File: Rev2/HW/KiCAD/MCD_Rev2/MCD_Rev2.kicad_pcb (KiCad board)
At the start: 2 copper layers, 196.3 x 114.9 mm, 76 parts, among them J1 DBUS_LOW, J2 DBUS_HIGH, J3 ABUS, J4 POWER, J5 JTAG, J6 Conn_01x02_Male, J7 DUART A, J8 DUART B, SW1 SW_Push, U1 XC9572XL-PC44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

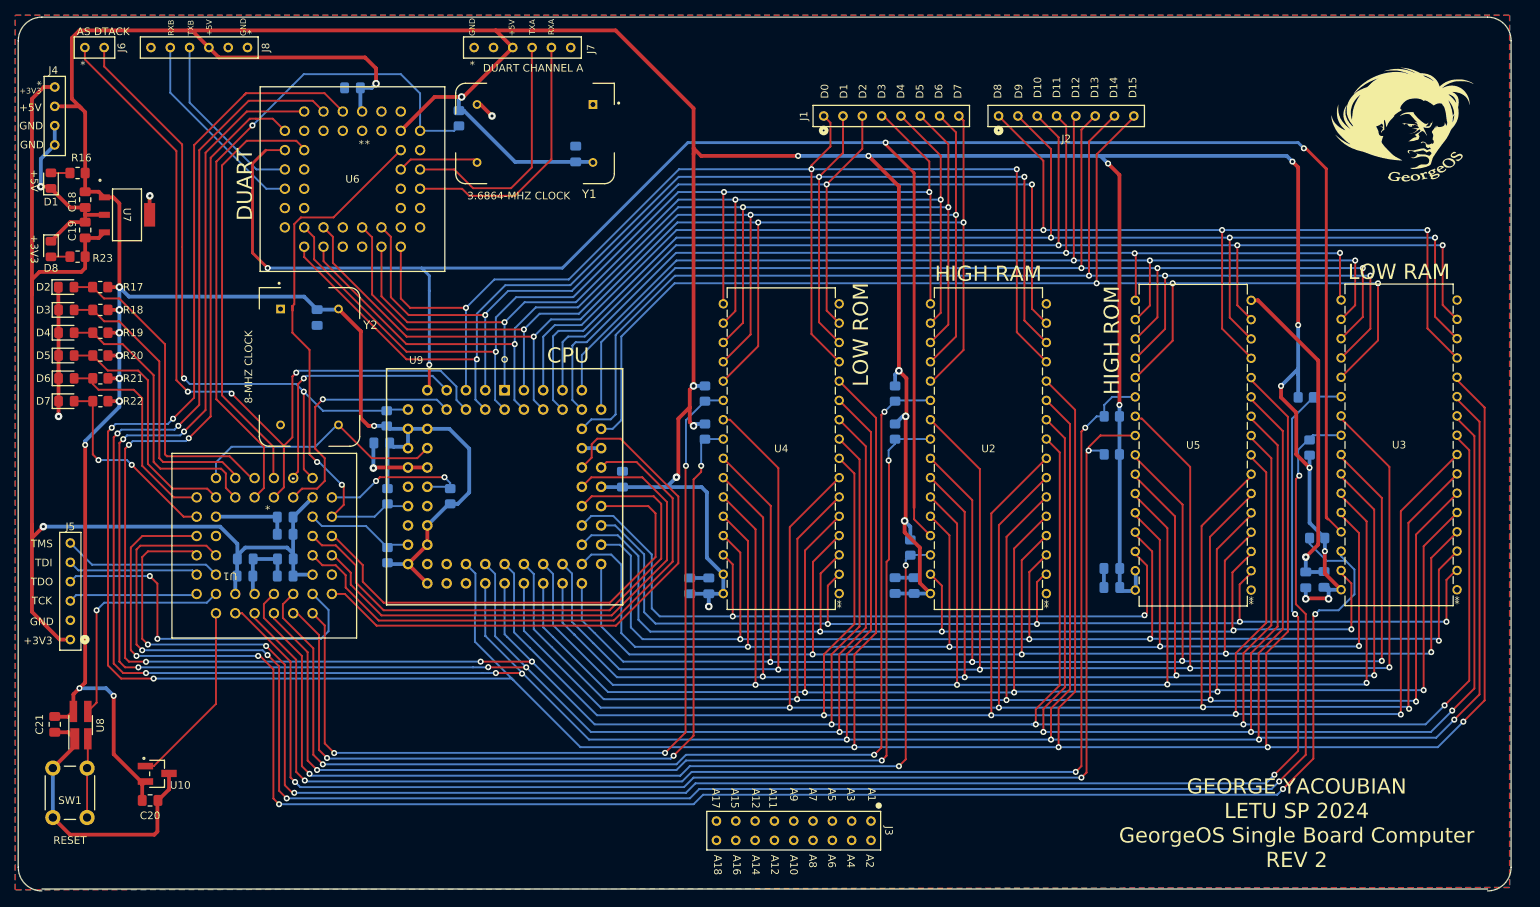
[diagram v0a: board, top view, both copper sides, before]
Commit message: started via stitching
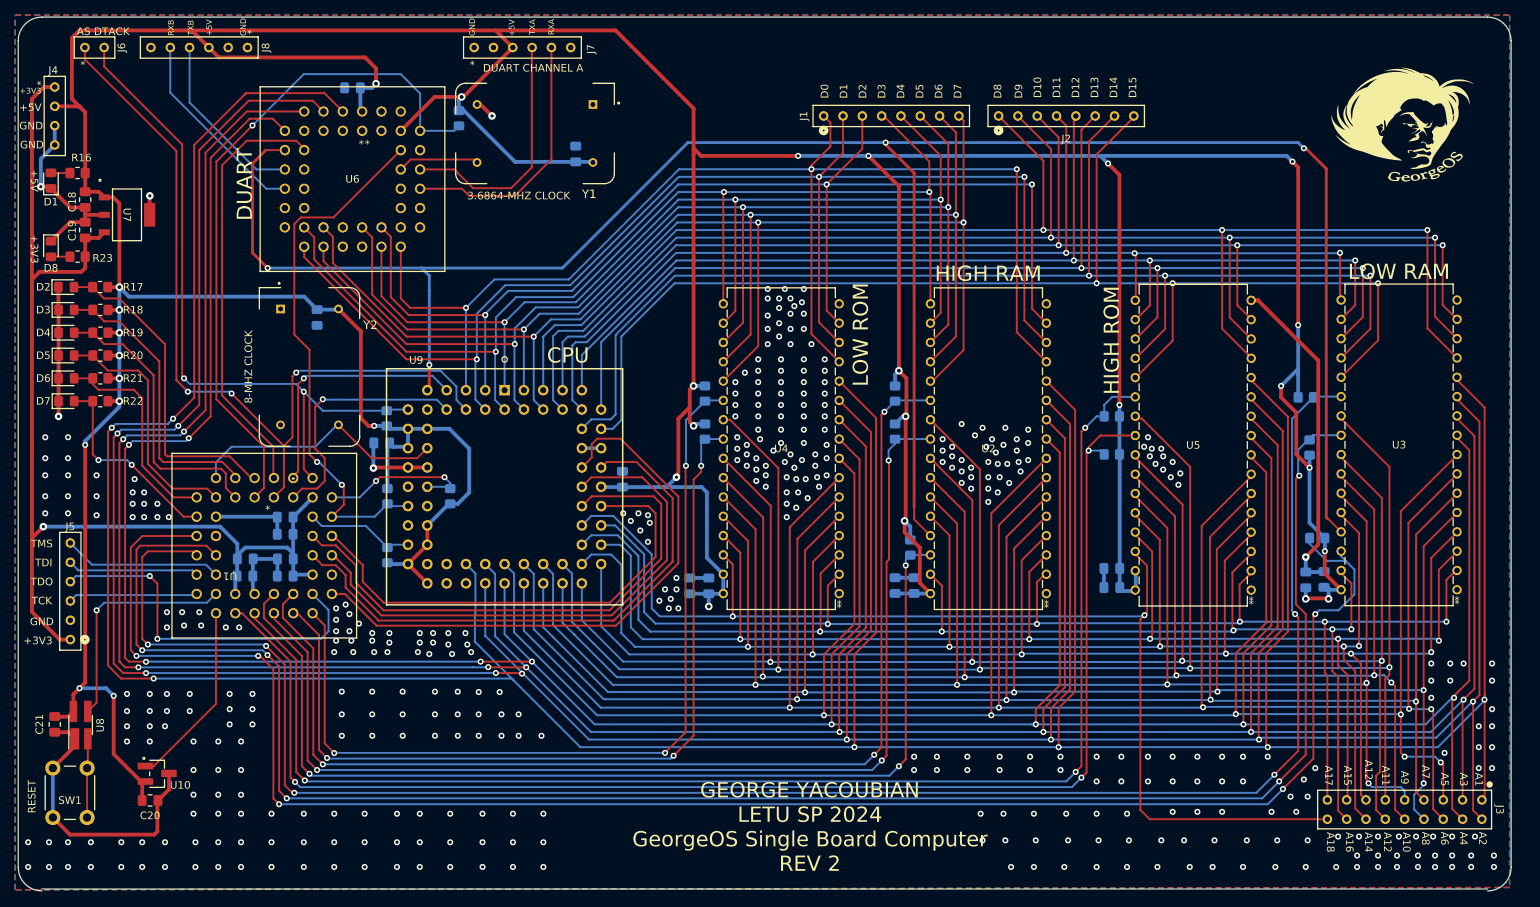
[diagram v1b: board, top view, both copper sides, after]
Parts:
- moved J3 80.4 mm to (283.0, 175.7)
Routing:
- net A18: track 101.7 -> 152.6 mm
- net A16: track 150.6 -> 176.3 mm, vias 4 -> 5
- net A14: track 186.8 -> 210.7 mm, vias 4 -> 5
- net A17: track 149.6 -> 173.2 mm, vias 4 -> 5
- net A15: track 174.8 -> 196.5 mm, vias 4 -> 5
- net A12: track 229.5 -> 251.1 mm
- net A10: track 228.1 -> 249.5 mm, vias 4 -> 5
- net A13: track 187.1 -> 207.2 mm, vias 4 -> 5
- net A9: track 224.2 -> 243.9 mm, vias 4 -> 5
- net A6: track 259.2 -> 277.2 mm, vias 4 -> 5
- net A8: track 225.2 -> 243.2 mm, vias 4 -> 5
- net A11: track 262.2 -> 279.9 mm
- net A4: track 434.9 -> 451.7 mm
- net A2: track 478.5 -> 494.5 mm
- net A5: track 277.0 -> 292.9 mm, vias 4 -> 6
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
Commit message: finished signals and power, need to via stitch
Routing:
- net GND: track 170.4 -> 108.9 mm, vias 428 -> 8
- net RAMHCE: track 242.1 -> 294.6 mm, vias 5 -> 3
- net RAMHCE2: track 237.3 -> 227.3 mm
- net RAMHOE: track 245.1 -> 235.5 mm
- net ROMLCE: track 113.9 -> 104.8 mm, vias 3 -> 1
- net ROMHOE: track 183.1 -> 174.2 mm, vias 3 -> 1
- net ROMLOE: track 112.7 -> 103.8 mm, vias 3 -> 1
- net ROMHCE: track 181.6 -> 173.0 mm, vias 3 -> 1
- net RAMLCE2: track 135.8 -> 127.3 mm, vias 3 -> 1
- net RAMLOE: track 145.4 -> 137.0 mm, vias 3 -> 1
- net RAMLCE: track 150.8 -> 142.6 mm, vias 3 -> 1
- net +5V: track 776.9 -> 771.7 mm, vias 30 -> 27
- net LED4: track 28.8 -> 28.2 mm
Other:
- board size 196.3 x 114.9 mm -> 196.3 x 114.7 mm
- board text added: "GEORGE YACOUBIAN LETU SU 2024 GeorgeOS Single Board Computer REV 3"
- board text removed: "GEORGE YACOUBIAN LETU SP 2024 GeorgeOS Single Board Computer REV 2"

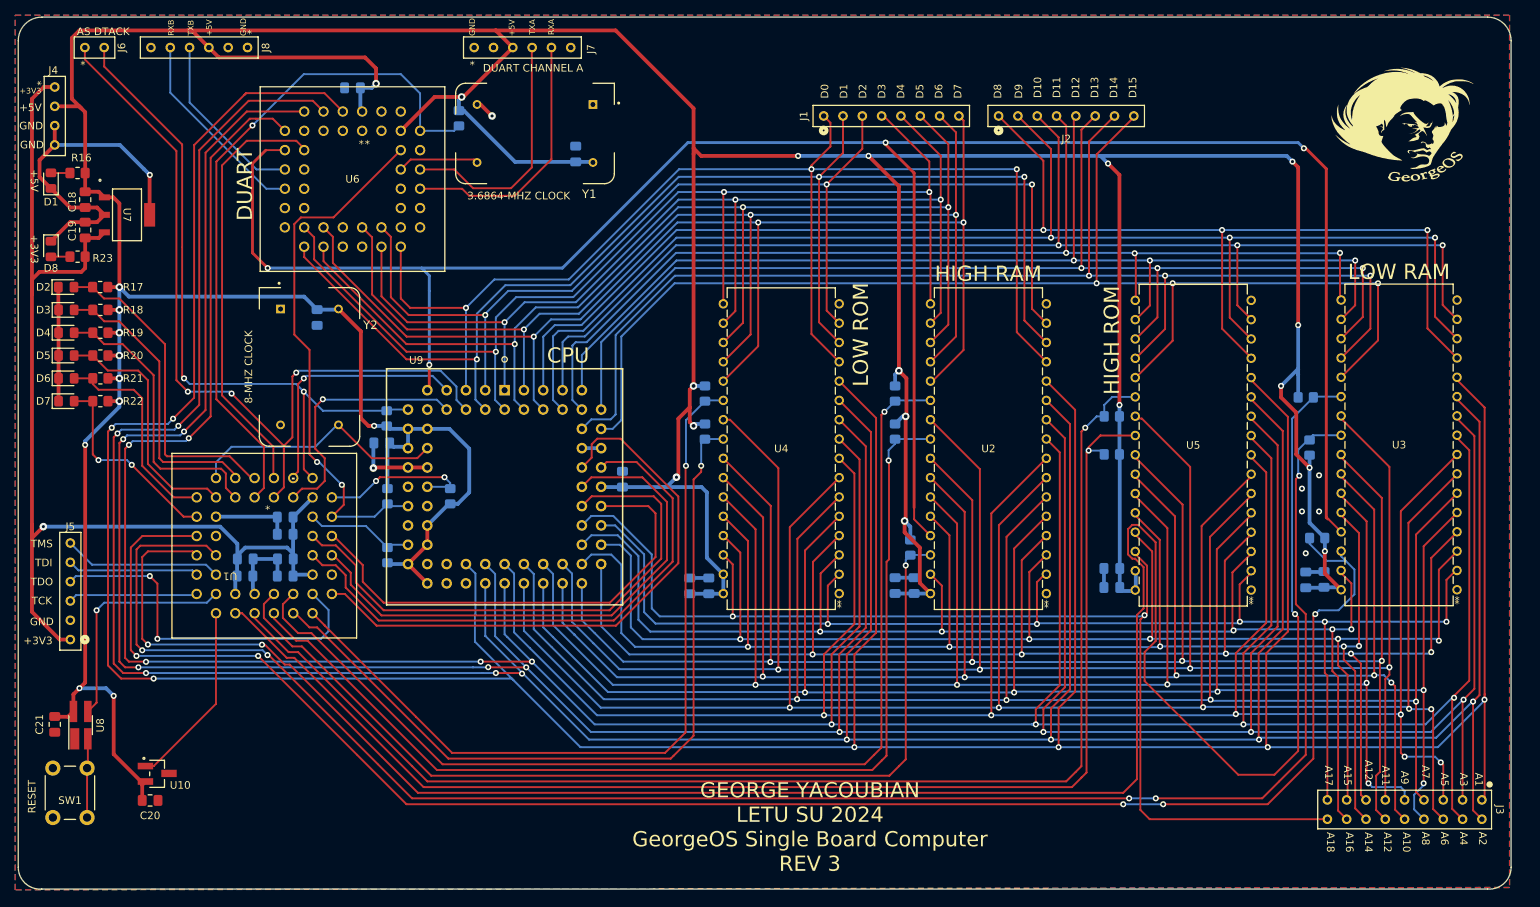
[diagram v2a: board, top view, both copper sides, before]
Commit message: spaced out traces
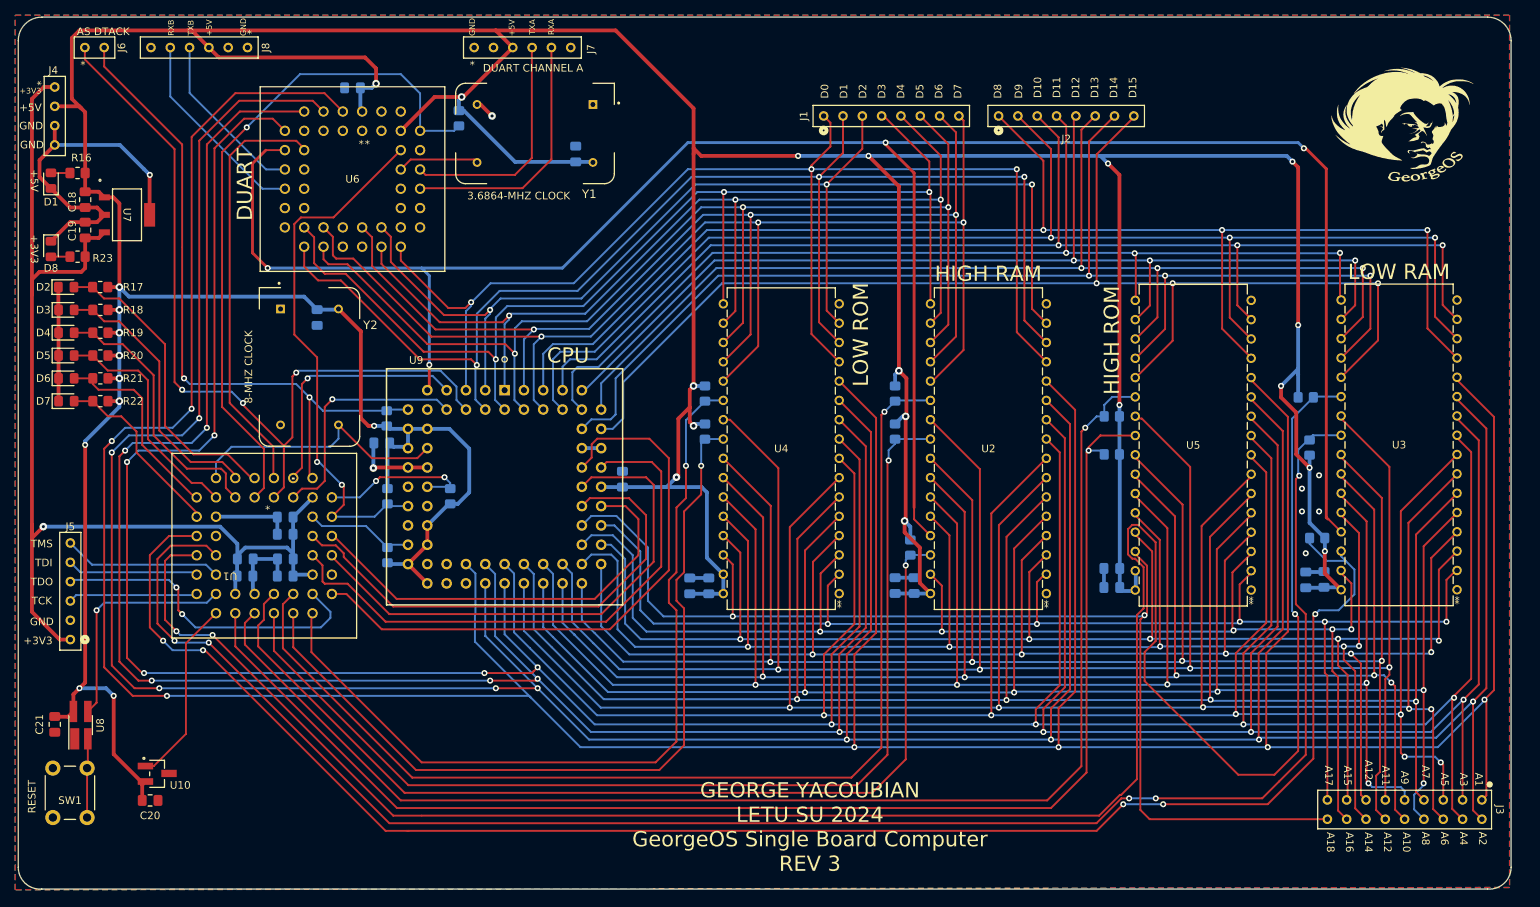
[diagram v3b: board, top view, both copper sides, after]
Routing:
- net A19: track 63.3 -> 56.5 mm
- net A20: track 72.6 -> 66.1 mm
- net ROMHCE: track 173.0 -> 178.9 mm
- net RAMHCE: track 294.6 -> 288.9 mm
- net A1: track 518.1 -> 523.3 mm
- net RAMHOE: track 235.5 -> 230.4 mm
- net RAMLCE2: track 127.3 -> 132.5 mm
- net ROMLCE: track 104.8 -> 109.9 mm
- net TDO: track 48.1 -> 43.1 mm
- net A2: track 494.5 -> 499.4 mm
- net ROMHOE: track 174.2 -> 179.0 mm
- net ROMLOE: track 103.8 -> 108.5 mm
- net RAMHCE2: track 227.3 -> 222.9 mm
- net RAMLOE: track 137.0 -> 141.1 mm
- net RAMLCE: track 142.6 -> 146.4 mm
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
